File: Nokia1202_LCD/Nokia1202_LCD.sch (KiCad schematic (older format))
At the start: 5 parts, among them P1 CONN_01X08

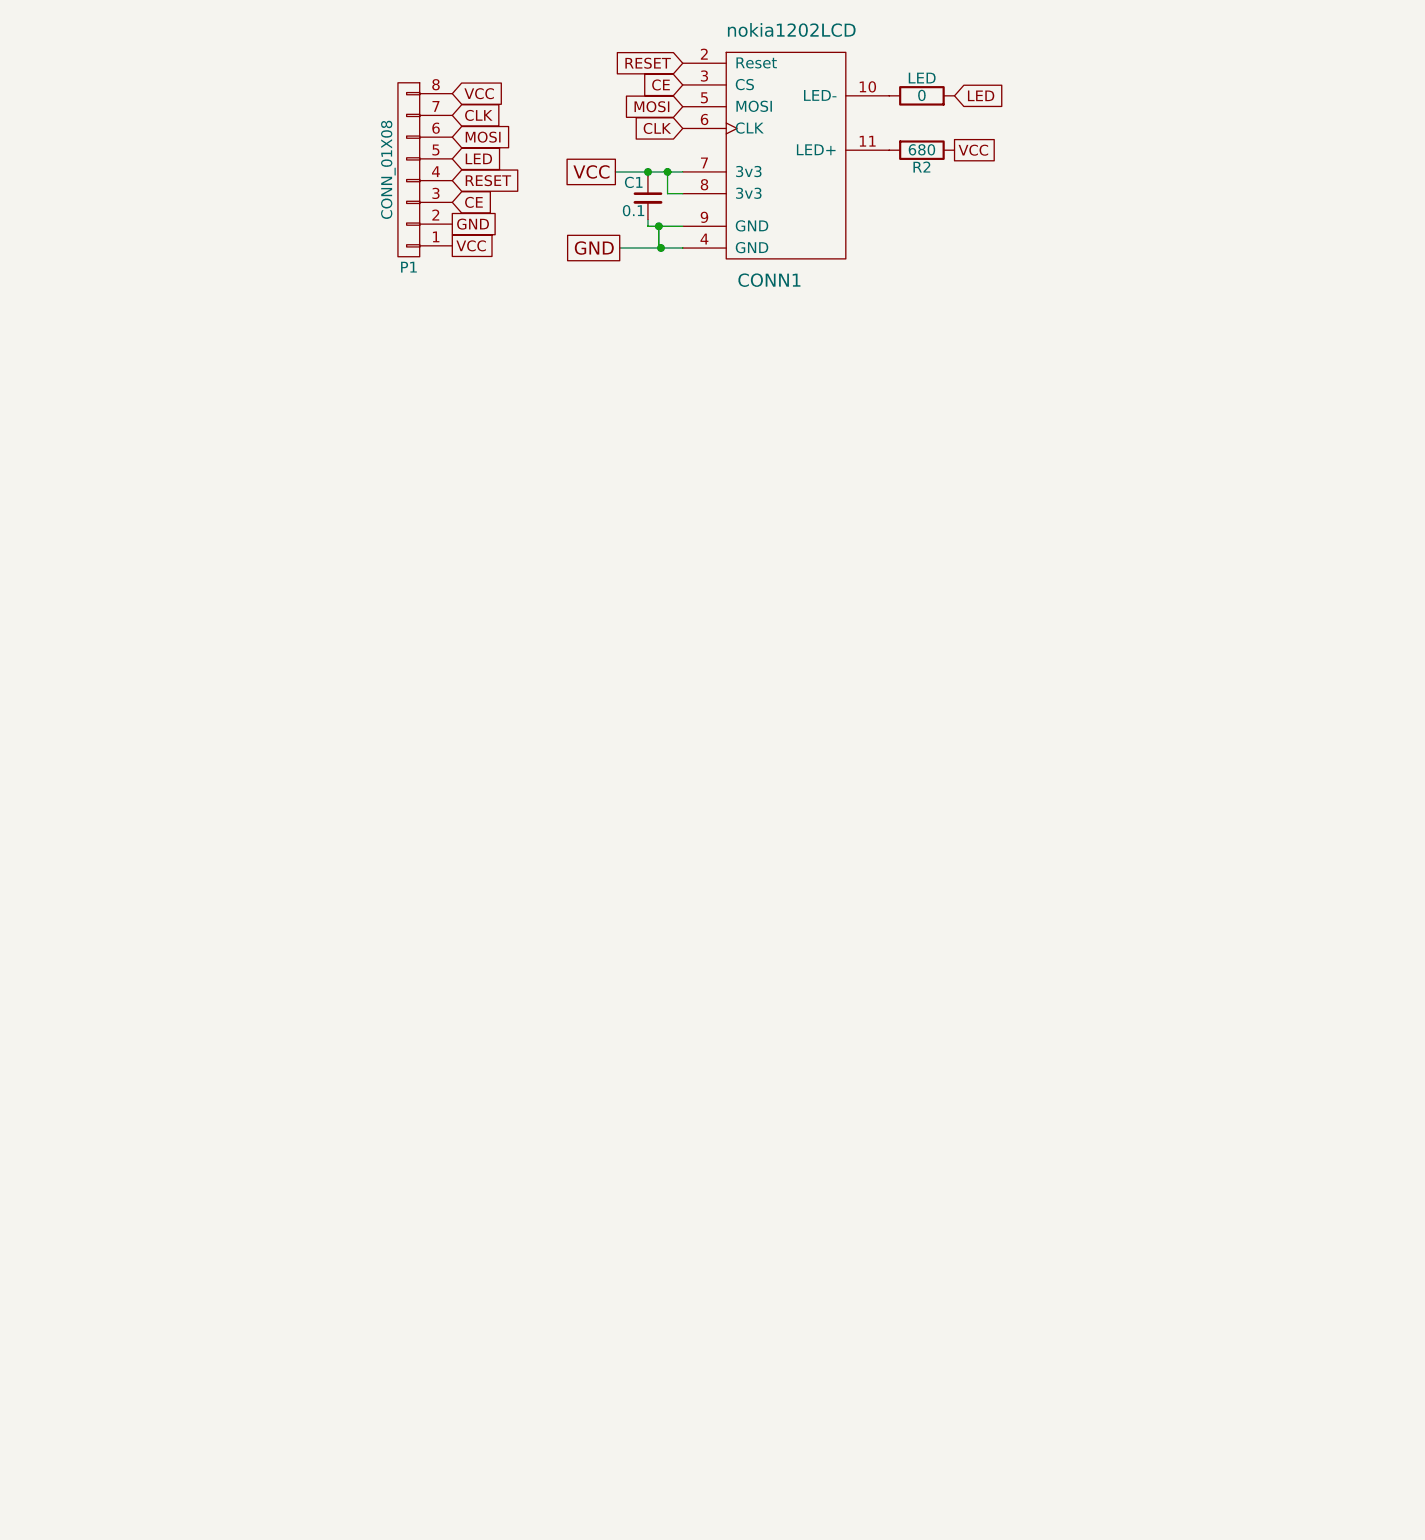
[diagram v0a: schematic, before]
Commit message: Re-rout PCB for Nokia1202 LCD breakout board
Re-arrange the capacitor on vcc line and the 0ohm resistor on LED line
Re-route the signals
Add a bottom copper pour
Make the power routes thicker[0.4mm]
Resize the board smaller
Export schematic[PDF] and PCB layout[SVG] for prototyping
Export PNG image of the 3D view
Delete an unsed image of an LCD pinout
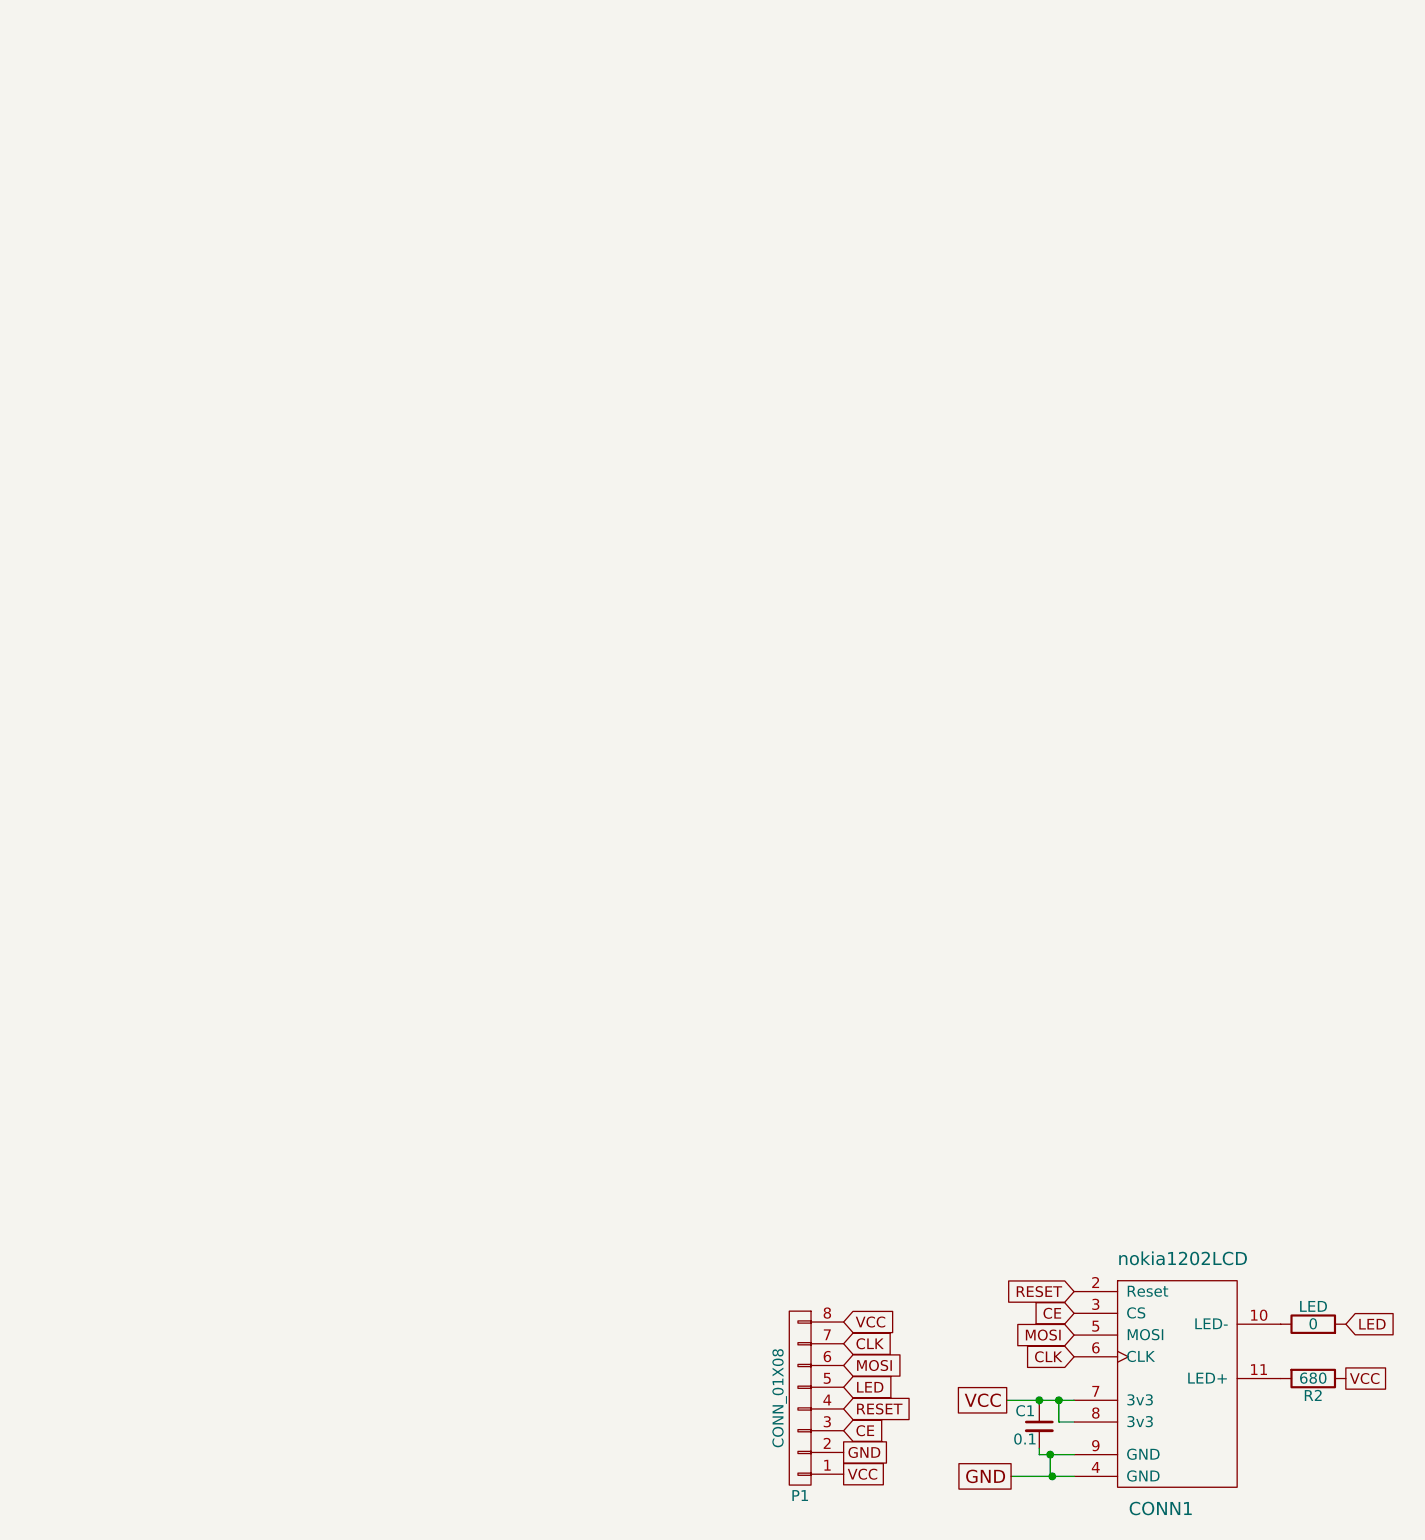
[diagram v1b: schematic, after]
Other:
- moved on the sheet: C1, CONN1, LED, P1, R2
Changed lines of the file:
@@
 EELAYER 25 0
 EELAYER END
-$Descr A4 11693 8268
+$Descr A4 8268 11693 portrait
 encoding utf-8
 Sheet 1 1
-Title ""
-Date ""
-Rev ""
-Comp ""
-Comment1 ""
-Comment2 ""
+Title "Nokia 1202 LCD Standard Breakout"
+Date "2018-01-24"
+Rev "1"
+Comp "Karibe"
+Comment1 "@muriukidavid"
+Comment2 "Karibe.co.ke"
 Comment3 ""
 Comment4 ""
 $EndDescr
-Text GLabel 3320 2890 0    60   UnSpc ~ 0
+Text GLabel 5120 8540 0    60   UnSpc ~ 0
 VCC
-Text GLabel 3340 3240 0    60   UnSpc ~ 0
+Text GLabel 5140 8890 0    60   UnSpc ~ 0
 GND
 $Comp
 L nokia1202LCD CONN1
 U 1 1 5887E9AD
-P 4130 2340
-F 0 "CONN1" H 4030 1290 60  0000 C CNN
-F 1 "nokia1202LCD" H 4130 2440 60  0000 C CNN
-F 2 "Connect:Nokia1202LCD" H 4130 2340 60  0001 C CNN
-F 3 "" H 4130 2340 60  0001 C CNN
-	1    4130 2340
+P 5930 7990
+F 0 "CONN1" H 5830 6940 60  0000 C CNN
+F 1 "nokia1202LCD" H 5930 8090 60  0000 C CNN
+F 2 "Connect:Nokia1202LCD" H 5930 7990 60  0001 C CNN
+F 3 "" H 5930 7990 60  0001 C CNN
+	1    5930 7990
 	1    0    0    -1
 $EndComp
-Text GLabel 2570 3230 2    49   UnSpc ~ 0
+Text GLabel 4370 8880 2    49   UnSpc ~ 0
 VCC
 $Comp
 L CONN_01X08 P1
 U 1 1 5887EAD6
-P 2370 2880
-F 0 "P1" H 2370 3330 50  0000 C CNN
-F 1 "CONN_01X08" V 2470 2880 50  0000 C CNN
-F 2 "Pin_Headers:Pin_Header_Straight_1x08" H 2370 2880 50  0001 C CNN
-F 3 "" H 2370 2880 50  0000 C CNN
-	1    2370 2880
+P 4170 8530
+F 0 "P1" H 4170 8980 50  0000 C CNN
+F 1 "CONN_01X08" V 4270 8530 50  0000 C CNN
+F 2 "Pin_Headers:Pin_Header_Straight_1x08" H 4170 8530 50  0001 C CNN
+F 3 "" H 4170 8530 50  0000 C CNN
+	1    4170 8530
 	-1   0    0    1
 $EndComp
-Text GLabel 2570 3130 2    49   UnSpc ~ 0
+Text GLabel 4370 8780 2    49   UnSpc ~ 0
 GND
-Text GLabel 2570 2930 2    49   Input ~ 0
+Text GLabel 4370 8580 2    49   Input ~ 0
 RESET
-Text GLabel 3630 2490 0    49   Input ~ 0
+Text GLabel 5430 8140 0    49   Input ~ 0
 CE
-Text GLabel 2570 3030 2    49   Input ~ 0
+Text GLabel 4370 8680 2    49   Input ~ 0
 CE
-Text GLabel 3630 2390 0    49   Input ~ 0
+Text GLabel 5430 8040 0    49   Input ~ 0
 RESET
-Text GLabel 2570 2730 2    49   Input ~ 0
+Text GLabel 4370 8380 2    49   Input ~ 0
 MOSI
-Text GLabel 2570 2630 2    49   Input ~ 0
+Text GLabel 4370 8280 2    49   Input ~ 0
 CLK
-Text GLabel 2570 2530 2    49   Input ~ 0
+Text GLabel 4370 8180 2    49   Input ~ 0
 VCC
-Text GLabel 3630 2590 0    49   Input ~ 0
+Text GLabel 5430 8240 0    49   Input ~ 0
 MOSI
-Text GLabel 3630 2690 0    49   Input ~ 0
+Text GLabel 5430 8340 0    49   Input ~ 0
 CLK
 $Comp
 L R R2
 U 1 1 5887EC97
-P 4730 2790
-F 0 "R2" V 4810 2790 50  0000 C CNN
-F 1 "680" V 4730 2790 50  0000 C CNN
-F 2 "Resistors_SMD:R_1206" V 4660 2790 50  0001 C CNN
-F 3 "" H 4730 2790 50  0000 C CNN
-	1    4730 2790
+P 6530 8440
+F 0 "R2" V 6610 8440 50  0000 C CNN
+F 1 "680" V 6530 8440 50  0000 C CNN
+F 2 "Resistors_SMD:R_1206" V 6460 8440 50  0001 C CNN
+F 3 "" H 6530 8440 50  0000 C CNN
+	1    6530 8440
 	0    1    1    0
 $EndComp
-Text GLabel 4880 2790 2    49   UnSpc ~ 0
+Text GLabel 6680 8440 2    49   UnSpc ~ 0
 VCC
 $Comp
 L C_Small C1
 U 1 1 5887EE6D
-P 3470 3010
-F 0 "C1" H 3360 3080 50  0000 L CNN
-F 1 "0.1" H 3350 2950 50  0000 L CNN
-F 2 "Capacitors_SMD:C_1206" H 3470 3010 50  0001 C CNN
-F 3 "" H 3470 3010 50  0000 C CNN
-	1    3470 3010
+P 5270 8660
+F 0 "C1" H 5160 8730 50  0000 L CNN
+F 1 "0.1" H 5150 8600 50  0000 L CNN
+F 2 "Capacitors_SMD:C_1206" H 5270 8660 50  0001 C CNN
+F 3 "" H 5270 8660 50  0000 C CNN
+	1    5270 8660
 	1    0    0    -1
 $EndComp
 Wire Wire Line
-	3340 3240 3630 3240
+	5140 8890 5430 8890
 Wire Wire Line
-	3630 3140 3470 3140
+	5430 8790 5270 8790
 Wire Wire Line
-	3470 3140 3470 3110
+	5270 8790 5270 8760
 Wire Wire Line
-	3520 3140 3520 3240
+	5320 8790 5320 8890
 Wire Wire Line
-	3520 3240 3530 3240
-Connection ~ 3530 3240
-Connection ~ 3520 3140
+	5320 8890 5330 8890
+Connection ~ 5330 8890
+Connection ~ 5320 8790
 Wire Wire Line
-	3320 2890 3630 2890
+	5120 8540 5430 8540
 Wire Wire Line
-	3470 2910 3470 2890
-Connection ~ 3470 2890
-Text GLabel 2570 2830 2    49   Input ~ 0
+	5270 8560 5270 8540
+Connection ~ 5270 8540
+Text GLabel 4370 8480 2    49   Input ~ 0
 LED
-Text GLabel 4880 2540 2    49   Input ~ 0
+Text GLabel 6680 8190 2    49   Input ~ 0
 LED
 $Comp
 L R LED
 U 1 1 5887F3A6
-P 4730 2540
-F 0 "LED" V 4810 2540 50  0000 C CNN
-F 1 "0" V 4730 2540 50  0000 C CNN
-F 2 "Resistors_SMD:R_1206" V 4660 2540 50  0001 C CNN
-F 3 "" H 4730 2540 50  0000 C CNN
-	1    4730 2540
+P 6530 8190
+F 0 "LED" V 6610 8190 50  0000 C CNN
+F 1 "0" V 6530 8190 50  0000 C CNN
+F 2 "Resistors_SMD:R_1206" V 6460 8190 50  0001 C CNN
+F 3 "" H 6530 8190 50  0000 C CNN
+	1    6530 8190
 	0    -1   -1   0
 $EndComp
 Wire Wire Line
-	3560 2890 3560 2990
+	5360 8540 5360 8640
 Wire Wire Line
-	3560 2990 3630 2990
-Connection ~ 3560 2890
+	5360 8640 5430 8640
+Connection ~ 5360 8540
 $EndSCHEMATC

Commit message: Clean up the simulation folders
Remove a duplicate amplifier simulation project amplifier in favor of the opamp of the project
Remove uneccesary files in the opamp
Add a README.md to explain how to use the RC circuit simulation netlist file for the filter's characteristics and sample signal input and output
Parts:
- C1: symbol C_Small -> device:C_Small
- CONN1: symbol nokia1202LCD -> Nokia1202_LCD-rescue:nokia1202LCD-RESCUE-Nokia1202_LCD
- LED, R2: symbol R -> device:R
- P1: symbol CONN_01X08 -> Nokia1202_LCD-rescue:CONN_01X08-RESCUE-Nokia1202_LCD
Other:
- moved on the sheet: C1, CONN1, LED, P1, R2
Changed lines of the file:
@@
 EESchema Schematic File Version 2
-LIBS:power
-LIBS:device
-LIBS:transistors
-LIBS:conn
-LIBS:linear
-LIBS:regul
-LIBS:74xx
-LIBS:cmos4000
-LIBS:adc-dac
-LIBS:memory
-LIBS:xilinx
-LIBS:microcontrollers
-LIBS:dsp
-LIBS:microchip
-LIBS:analog_switches
-LIBS:motorola
-LIBS:texas
-LIBS:intel
-LIBS:audio
-LIBS:interface
-LIBS:digital-audio
-LIBS:philips
-LIBS:display
-LIBS:cypress
-LIBS:siliconi
-LIBS:opto
-LIBS:atmel
-LIBS:contrib
-LIBS:valves
+LIBS:justVI-components
 LIBS:Nokia1202_LCD-cache
 EELAYER 25 0
 EELAYER END
-$Descr A4 8268 11693 portrait
+$Descr User 5512 6299
 encoding utf-8
 Sheet 1 1
 Title "Nokia 1202 LCD Standard Breakout"
-Date "2018-01-24"
+Date "2018-04-24"
 Rev "1"
 Comp "Karibe"
@@
 Comment4 ""
 $EndDescr
-Text GLabel 5120 8540 0    60   UnSpc ~ 0
+Text GLabel 2470 2925 0    60   UnSpc ~ 0
 VCC
-Text GLabel 5140 8890 0    60   UnSpc ~ 0
+Text GLabel 2490 3275 0    60   UnSpc ~ 0
 GND
 $Comp
-L nokia1202LCD CONN1
+L Nokia1202_LCD-rescue:nokia1202LCD-RESCUE-Nokia1202_LCD CONN1
 U 1 1 5887E9AD
-P 5930 7990
-F 0 "CONN1" H 5830 6940 60  0000 C CNN
-F 1 "nokia1202LCD" H 5930 8090 60  0000 C CNN
-F 2 "Connect:Nokia1202LCD" H 5930 7990 60  0001 C CNN
-F 3 "" H 5930 7990 60  0001 C CNN
-	1    5930 7990
+P 3280 2375
+F 0 "CONN1" H 3180 1325 60  0000 C CNN
+F 1 "nokia1202LCD" H 3280 2475 60  0000 C CNN
+F 2 "Connect:Nokia1202LCD" H 3280 2375 60  0001 C CNN
+F 3 "" H 3280 2375 60  0001 C CNN
+	1    3280 2375
 	1    0    0    -1
 $EndComp
-Text GLabel 4370 8880 2    49   UnSpc ~ 0
+Text GLabel 1720 3265 2    49   UnSpc ~ 0
 VCC
 $Comp
-L CONN_01X08 P1
+L Nokia1202_LCD-rescue:CONN_01X08-RESCUE-Nokia1202_LCD P1
 U 1 1 5887EAD6
-P 4170 8530
-F 0 "P1" H 4170 8980 50  0000 C CNN
-F 1 "CONN_01X08" V 4270 8530 50  0000 C CNN
-F 2 "Pin_Headers:Pin_Header_Straight_1x08" H 4170 8530 50  0001 C CNN
-F 3 "" H 4170 8530 50  0000 C CNN
-	1    4170 8530
+P 1520 2915
+F 0 "P1" H 1520 3365 50  0000 C CNN
+F 1 "CONN_01X08" V 1620 2915 50  0000 C CNN
+F 2 "Pin_Headers:Pin_Header_Straight_1x08" H 1520 2915 50  0001 C CNN
+F 3 "" H 1520 2915 50  0000 C CNN
+	1    1520 2915
 	-1   0    0    1
 $EndComp
-Text GLabel 4370 8780 2    49   UnSpc ~ 0
+Text GLabel 1720 3165 2    49   UnSpc ~ 0
 GND
-Text GLabel 4370 8580 2    49   Input ~ 0
+Text GLabel 1720 2965 2    49   Input ~ 0
 RESET
-Text GLabel 5430 8140 0    49   Input ~ 0
+Text GLabel 2780 2525 0    49   Input ~ 0
 CE
-Text GLabel 4370 8680 2    49   Input ~ 0
+Text GLabel 1720 3065 2    49   Input ~ 0
 CE
-Text GLabel 5430 8040 0    49   Input ~ 0
+Text GLabel 2780 2425 0    49   Input ~ 0
 RESET
-Text GLabel 4370 8380 2    49   Input ~ 0
+Text GLabel 1720 2765 2    49   Input ~ 0
 MOSI
-Text GLabel 4370 8280 2    49   Input ~ 0
+Text GLabel 1720 2665 2    49   Input ~ 0
 CLK
-Text GLabel 4370 8180 2    49   Input ~ 0
+Text GLabel 1720 2565 2    49   Input ~ 0
 VCC
-Text GLabel 5430 8240 0    49   Input ~ 0
+Text GLabel 2780 2625 0    49   Input ~ 0
 MOSI
-Text GLabel 5430 8340 0    49   Input ~ 0
+Text GLabel 2780 2725 0    49   Input ~ 0
 CLK
 $Comp
-L R R2
+L device:R R2
 U 1 1 5887EC97
-P 6530 8440
-F 0 "R2" V 6610 8440 50  0000 C CNN
-F 1 "680" V 6530 8440 50  0000 C CNN
-F 2 "Resistors_SMD:R_1206" V 6460 8440 50  0001 C CNN
-F 3 "" H 6530 8440 50  0000 C CNN
-	1    6530 8440
+P 3880 2825
+F 0 "R2" V 3960 2825 50  0000 C CNN
+F 1 "680" V 3880 2825 50  0000 C CNN
+F 2 "Resistors_SMD:R_1206" V 3810 2825 50  0001 C CNN
+F 3 "" H 3880 2825 50  0000 C CNN
+	1    3880 2825
 	0    1    1    0
 $EndComp
-Text GLabel 6680 8440 2    49   UnSpc ~ 0
+Text GLabel 4030 2825 2    49   UnSpc ~ 0
 VCC
 $Comp
-L C_Small C1
+L device:C_Small C1
 U 1 1 5887EE6D
-P 5270 8660
-F 0 "C1" H 5160 8730 50  0000 L CNN
-F 1 "0.1" H 5150 8600 50  0000 L CNN
-F 2 "Capacitors_SMD:C_1206" H 5270 8660 50  0001 C CNN
-F 3 "" H 5270 8660 50  0000 C CNN
-	1    5270 8660
+P 2620 3045
+F 0 "C1" H 2510 3115 50  0000 L CNN
+F 1 "0.1" H 2500 2985 50  0000 L CNN
+F 2 "Capacitors_SMD:C_1206" H 2620 3045 50  0001 C CNN
+F 3 "" H 2620 3045 50  0000 C CNN
+	1    2620 3045
 	1    0    0    -1
 $EndComp
 Wire Wire Line
-	5140 8890 5430 8890
+	2620 3175 2780 3175
 Wire Wire Line
-	5430 8790 5270 8790
+	2620 3175 2620 3145
 Wire Wire Line
-	5270 8790 5270 8760
+	2470 2925 2780 2925
 Wire Wire Line
-	5320 8790 5320 8890
-Wire Wire Line
-	5320 8890 5330 8890
-Connection ~ 5330 8890
-Connection ~ 5320 8790
-Wire Wire Line
-	5120 8540 5430 8540
-Wire Wire Line
-	5270 8560 5270 8540
-Connection ~ 5270 8540
-Text GLabel 4370 8480 2    49   Input ~ 0
+	2620 2925 2620 2945
+Connection ~ 2620 2925
+Text GLabel 1720 2865 2    49   Input ~ 0
 LED
-Text GLabel 6680 8190 2    49   Input ~ 0
+Text GLabel 4030 2575 2    49   Input ~ 0
 LED
 $Comp
-L R LED
+L device:R LED
 U 1 1 5887F3A6
-P 6530 8190
-F 0 "LED" V 6610 8190 50  0000 C CNN
-F 1 "0" V 6530 8190 50  0000 C CNN
-F 2 "Resistors_SMD:R_1206" V 6460 8190 50  0001 C CNN
-F 3 "" H 6530 8190 50  0000 C CNN
-	1    6530 8190
+P 3880 2575
+F 0 "LED" V 3960 2575 50  0000 C CNN
+F 1 "0" V 3880 2575 50  0000 C CNN
+F 2 "Resistors_SMD:R_1206" V 3810 2575 50  0001 C CNN
+F 3 "" H 3880 2575 50  0000 C CNN
+	1    3880 2575
 	0    -1   -1   0
 $EndComp
 Wire Wire Line
-	5360 8540 5360 8640
+	2710 2925 2710 3025
 Wire Wire Line
-	5360 8640 5430 8640
-Connection ~ 5360 8540
+	2710 3025 2780 3025
+Connection ~ 2710 2925
+Wire Wire Line
+	2490 3275 2780 3275
+Wire Wire Line
+	2730 3275 2730 3175
+Wire Wire Line
+	2730 3175 2725 3175
+Connection ~ 2725 3175
+Connection ~ 2730 3275
 $EndSCHEMATC
